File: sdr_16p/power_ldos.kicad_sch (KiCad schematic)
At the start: 57 parts, among them U10 LT3042xMSE, U21 LT3045xMSE, U38 LT3042xMSE, U39 LT3042xMSE, U4 LT3042xMSE, U40 LT3042xMSE, U42 LT3045xMSE, U43 LT3045xMSE, U44 LT3045xMSE, U49 LT3045xMSE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

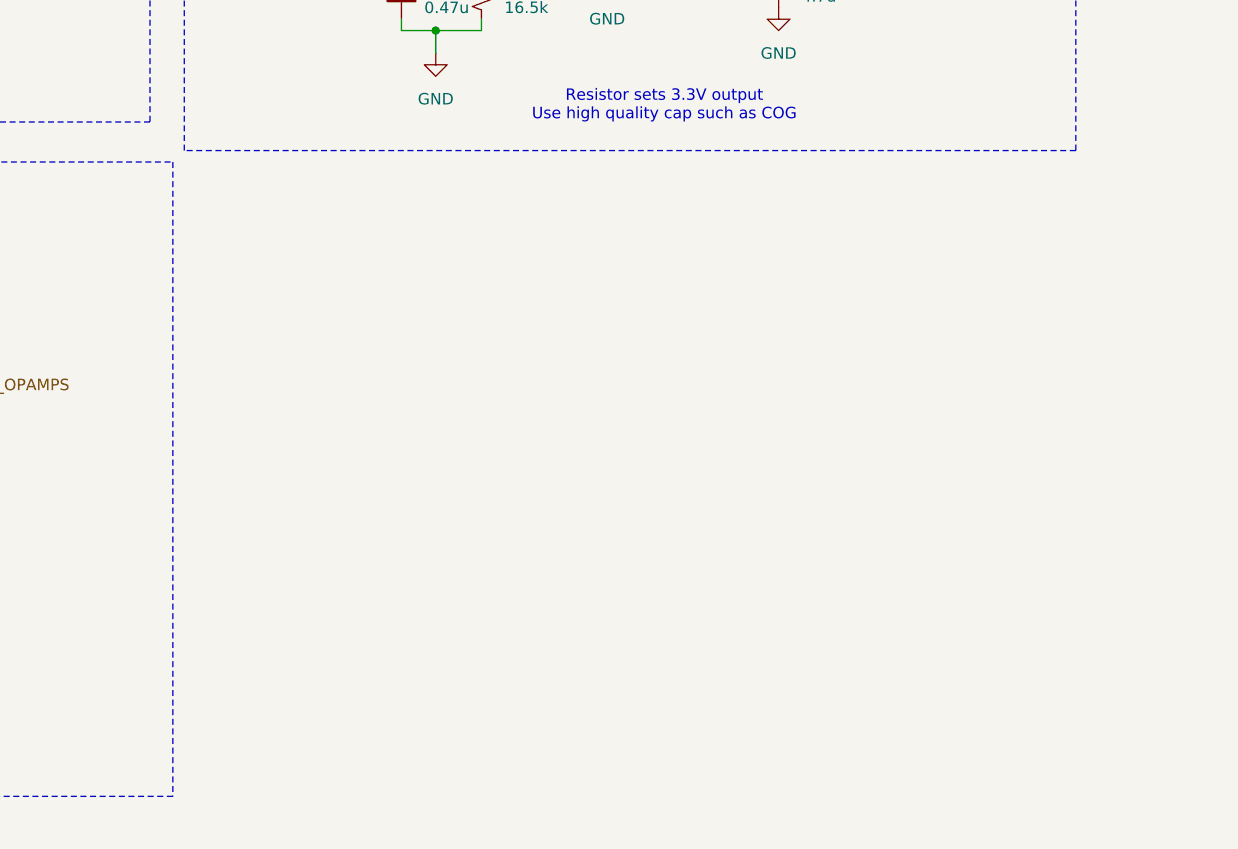
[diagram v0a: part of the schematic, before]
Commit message: back to 16 phases
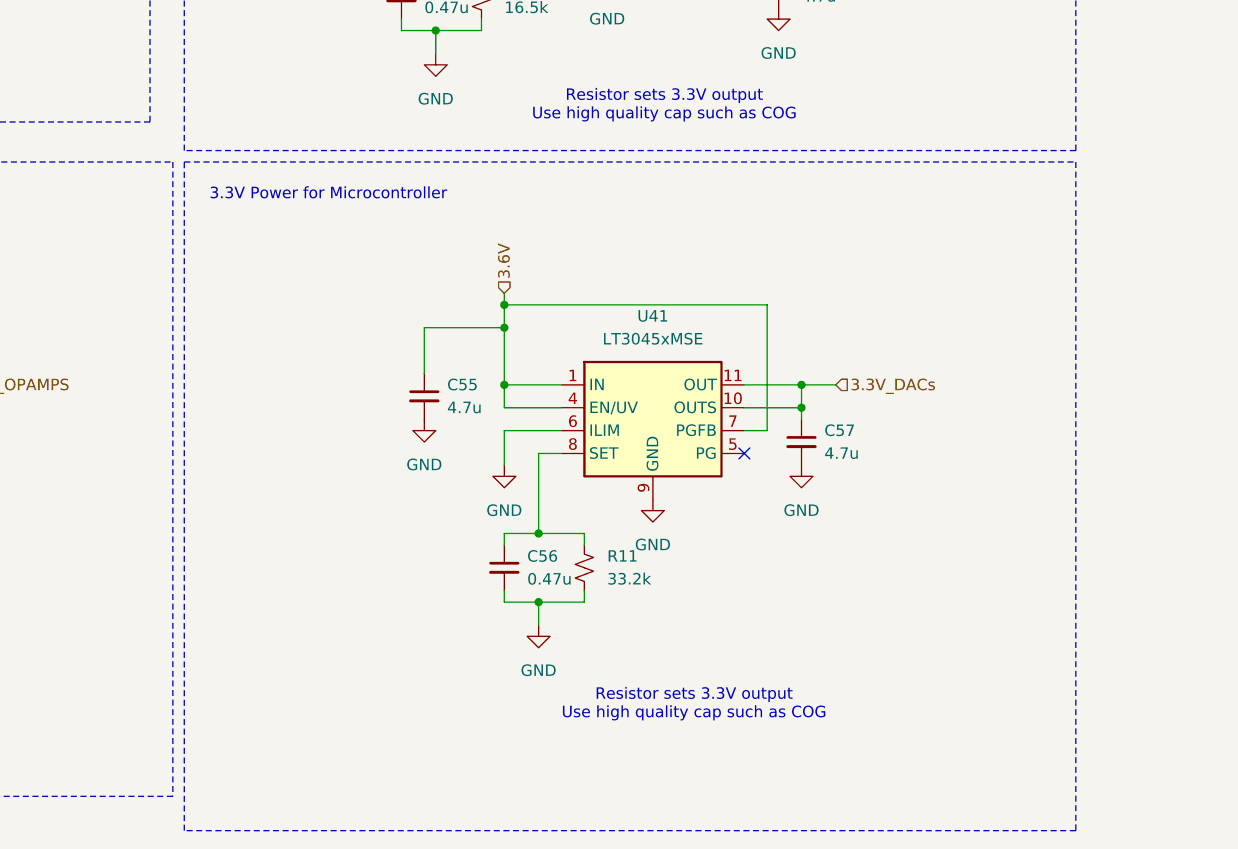
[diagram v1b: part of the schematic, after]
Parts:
- added C55, C57: 4.7u, Capacitor_SMD:C_0603_1608Metric_Pad1.08x0.95mm_HandSolder, symbol Device:C_Small
- added C56: 0.47u, Capacitor_SMD:C_0603_1608Metric_Pad1.08x0.95mm_HandSolder, symbol Device:C_Small
- added R11: 33.2k, Resistor_SMD:R_0603_1608Metric_Pad0.98x0.95mm_HandSolder, symbol Device:R_Small_US
- added U41: LT3045xMSE, Package_SO:MSOP-12-1EP_3x4.039mm_P0.65mm_EP1.651x2.845mm, symbol Regulator_Linear:LT3045xMSE
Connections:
- net 3.3V_DACs: now also C57.1, U41.10 (OUTS), U41.11 (OUT), U41.12 (OUT)
- net 3.6V: now also C55.1, U41.1 (IN), U41.2 (IN), U41.3 (IN), U41.4 (EN/UV), U41.7 (PGFB)
- net GND: now also C55.2, C56.2, C57.2, R11.2, U41.13 (GND), U41.6 (ILIM), U41.9 (GND)
- new net: C56.1, R11.1, U41.8 (SET)
- no-connect marks 12 -> 13
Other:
- note added: "3.3V Power for Microcontroller"
